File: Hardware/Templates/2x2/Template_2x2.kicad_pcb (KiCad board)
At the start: 2 copper layers, 84 x 84 mm, 4 parts

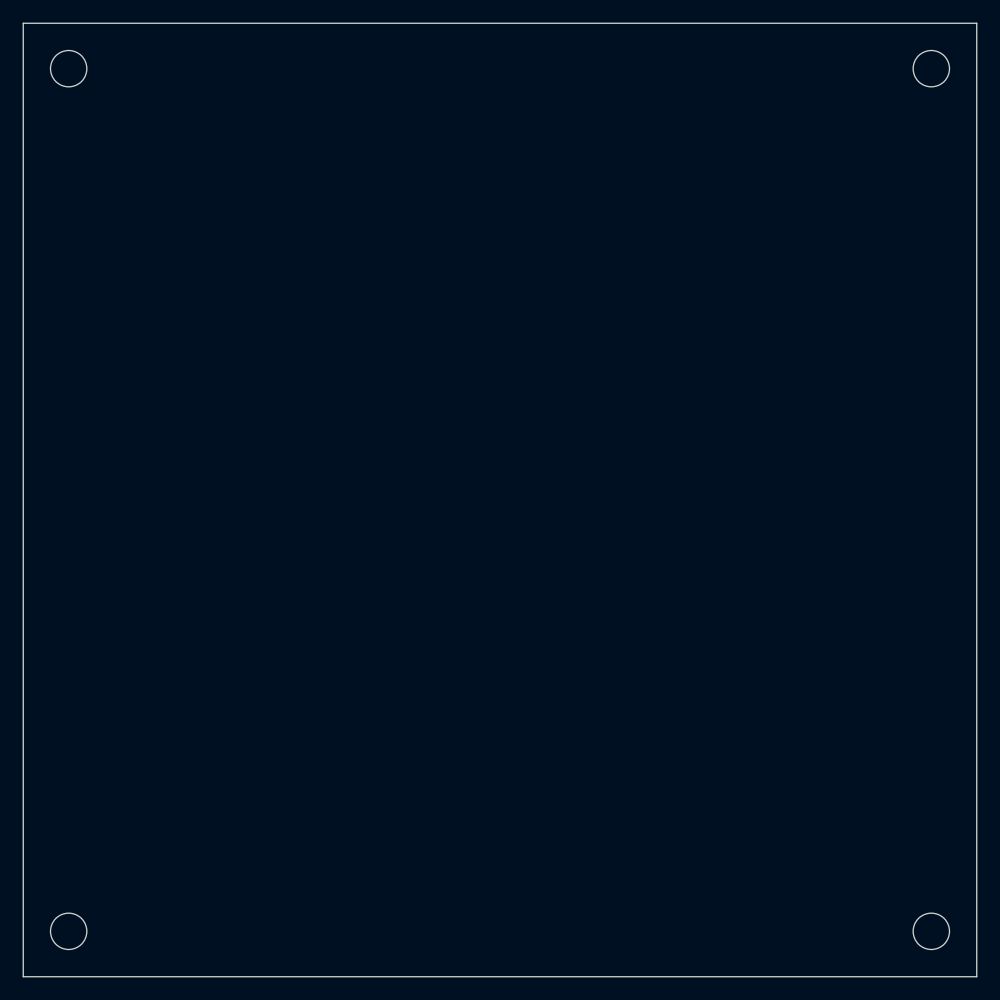
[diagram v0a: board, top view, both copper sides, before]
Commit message: Edited Templates for Hardware
Edited size of templates to fit within containers
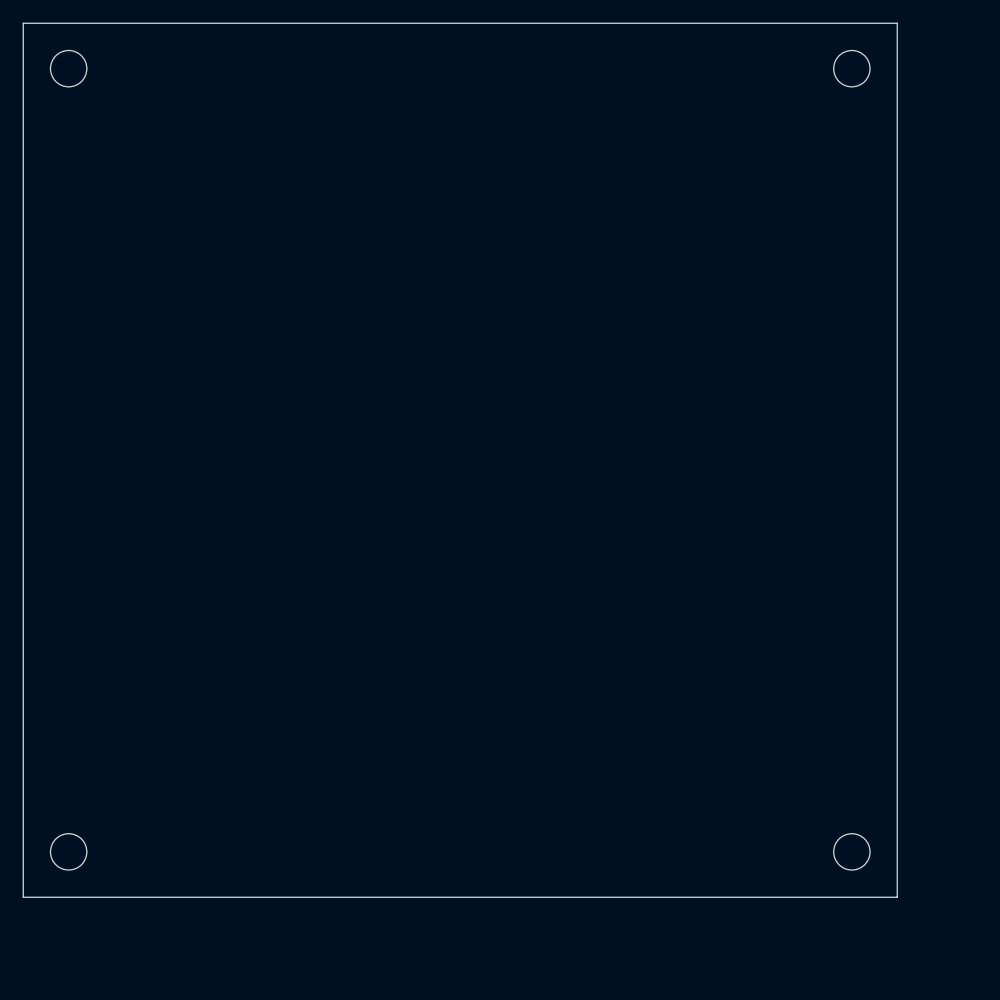
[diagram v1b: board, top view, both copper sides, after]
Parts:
- moved REF** 9.90 mm to (93.0, 93.0)
- moved REF** 7.00 mm to (93.0, 24.0)
- moved REF** 7.00 mm to (24.0, 93.0)
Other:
- board size 84 x 84 mm -> 77 x 77 mm
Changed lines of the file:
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@@
 	(footprint "MountingHole:MountingHole_3.2mm_M3"
 		(layer "F.Cu")
-		(at 100 100)
+		(at 93 93)
 		(descr "Mounting Hole 3.2mm, no annular, M3")
 		(tags "mounting hole 3.2mm no annular m3")
@@
 	(footprint "MountingHole:MountingHole_3.2mm_M3"
 		(layer "F.Cu")
-		(at 100 24)
+		(at 93 24)
 		(descr "Mounting Hole 3.2mm, no annular, M3")
 		(tags "mounting hole 3.2mm no annular m3")
@@
 	(footprint "MountingHole:MountingHole_3.2mm_M3"
 		(layer "F.Cu")
-		(at 24 100)
+		(at 24 93)
 		(descr "Mounting Hole 3.2mm, no annular, M3")
 		(tags "mounting hole 3.2mm no annular m3")
@@
 	(gr_rect
 		(start 20 20)
-		(end 104 104)
+		(end 97 97)
 		(stroke
 			(width 0.1)
